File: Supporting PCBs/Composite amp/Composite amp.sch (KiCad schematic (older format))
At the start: 10 parts, among them J1 Conn_01x14_Female, Q1 MMBT3906

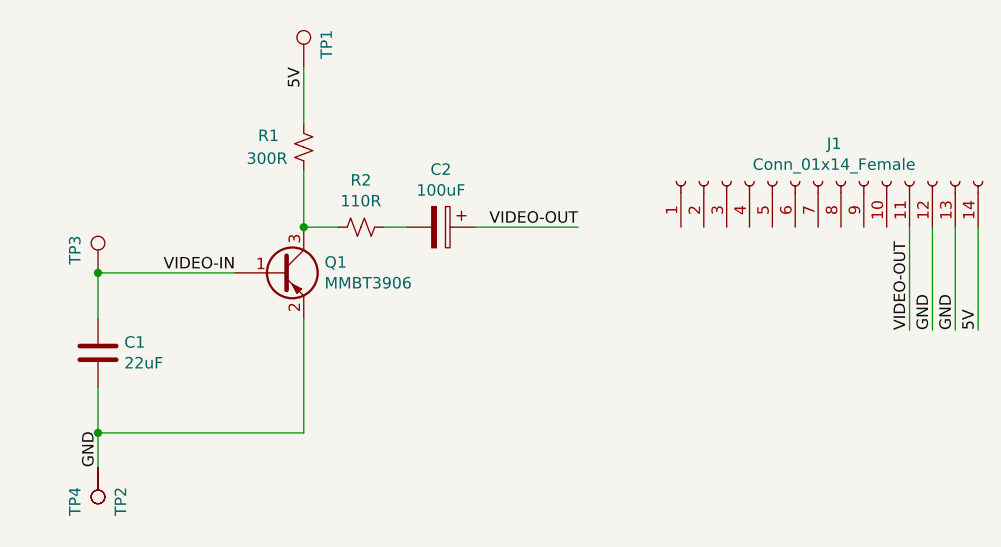
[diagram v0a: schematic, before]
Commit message: + Updated README.md + Fixed schematic/pinout error with Q1, and added decoupling capacitor to Composite Amp
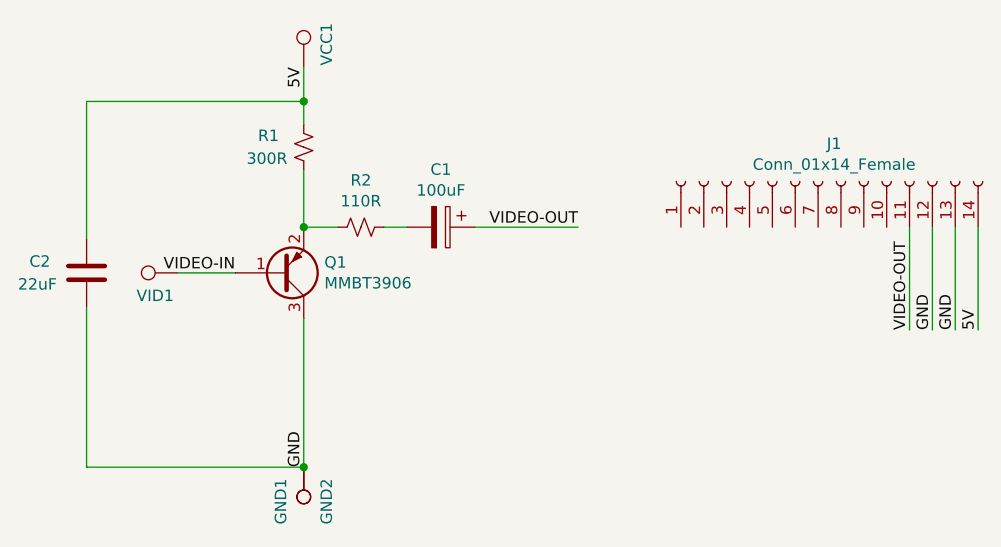
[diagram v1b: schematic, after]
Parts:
- removed C1: 22uF, Capacitor_SMD:C_0805_2012Metric, symbol Device:C
- added C2: 22uF, Capacitor_SMD:C_0805_2012Metric_Pad1.15x1.40mm_HandSolder, symbol Device:C
- renumbered C2 to C1, TP4 to GND1, TP2 to GND2, TP1 to VCC1, TP3 to VID1
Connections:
- net 5V: now also C2.1
- net GND: now also Q1.3 (C), C2.2; no longer Q1.2 (E)
- net at R1.2, R2.2: now also Q1.2 (E); no longer Q1.3 (C)
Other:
- moved on the sheet: GND1, GND2, VID1
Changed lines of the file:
@@
 Text Label 6300 2800 3    50   ~ 0
 5V
-Connection ~ 5400 4400
-Wire Wire Line
-	5400 4400 5400 4550
-Wire Wire Line
-	6300 3900 6300 4400
 $Comp
-L Connector:TestPoint TP2
+L Connector:TestPoint GND2
 U 1 1 6144479E
-P 5400 4550
-F 0 "TP2" V 5300 4700 50  0000 C CNN
-F 1 "TestPoint" V 5504 4622 50  0001 C CNN
-F 2 "TinyTendo:SolderPad" H 5600 4550 50  0001 C CNN
-F 3 "~" H 5600 4550 50  0001 C CNN
-	1    5400 4550
+P 6300 4550
+F 0 "GND2" V 6200 4700 50  0000 C CNN
+F 1 "TestPoint" V 6404 4622 50  0001 C CNN
+F 2 "TinyTendo:SolderPad" H 6500 4550 50  0001 C CNN
+F 3 "~" H 6500 4550 50  0001 C CNN
+	1    6300 4550
 	-1   0    0    1
 $EndComp
 $Comp
-L Connector:TestPoint TP3
+L Connector:TestPoint VID1
 U 1 1 61444DBD
-P 5400 3700
-F 0 "TP3" V 5300 3800 50  0000 C CNN
-F 1 "TestPoint" V 4400 3150 50  0001 C CNN
-F 2 "TinyTendo:SolderPad" H 5600 3700 50  0001 C CNN
-F 3 "~" H 5600 3700 50  0001 C CNN
-	1    5400 3700
-	1    0    0    -1
+P 5750 3700
+F 0 "VID1" V 5650 3800 50  0000 C CNN
+F 1 "TestPoint" V 4750 3150 50  0001 C CNN
+F 2 "TinyTendo:SolderPad" H 5950 3700 50  0001 C CNN
+F 3 "~" H 5950 3700 50  0001 C CNN
+	1    5750 3700
+	0    -1   -1   0
 $EndComp
 $Comp
@@
 5V
 Wire Wire Line
-	9050 3950 9050 3500
-Wire Wire Line
 	9150 3950 9150 3500
-Wire Wire Line
-	9250 3950 9250 3500
 Text Label 7500 3500 2    50   ~ 0
 VIDEO-OUT
@@
 Text Label 9150 3950 1    50   ~ 0
 GND
-Wire Wire Line
-	8950 3950 8950 3500
 Text Label 8950 3950 1    50   ~ 0
 VIDEO-OUT
 $Comp
-L Connector:TestPoint TP4
+L Connector:TestPoint GND1
 U 1 1 6142B86A
-P 5400 4550
-F 0 "TP4" V 5500 4700 50  0000 C CNN
-F 1 "TestPoint" V 5504 4622 50  0001 C CNN
-F 2 "TinyTendo:SolderPad" H 5600 4550 50  0001 C CNN
-F 3 "~" H 5600 4550 50  0001 C CNN
-	1    5400 4550
+P 6300 4550
+F 0 "GND1" V 6400 4700 50  0000 C CNN
+F 1 "TestPoint" V 6404 4622 50  0001 C CNN
+F 2 "TinyTendo:SolderPad" H 6500 4550 50  0001 C CNN
+F 3 "~" H 6500 4550 50  0001 C CNN
+	1    6300 4550
 	-1   0    0    1
 $EndComp
+Text Label 6300 4550 1    50   ~ 0
+GND
+Text Label 6000 3700 2    50   ~ 0
+VIDEO-IN
+Wire Wire Line
+	6300 2800 6300 2950
+Wire Wire Line
+	7050 3500 7500 3500
 $Comp
-L Device:C C1
-U 1 1 60214EBB
-P 5400 4050
-F 0 "C1" H 5515 4096 50  0000 L CNN
-F 1 "22uF" H 5515 4005 50  0000 L CNN
-F 2 "Capacitor_SMD:C_0805_2012Metric" H 5438 3900 50  0001 C CNN
-F 3 "~" H 5400 4050 50  0001 C CNN
-	1    5400 4050
-	1    0    0    -1
+L Device:CP C1
+U 1 1 6021CE25
+P 6900 3500
+F 0 "C1" V 6648 3500 50  0000 C CNN
+F 1 "100uF" V 6739 3500 50  0000 C CNN
+F 2 "Capacitor_SMD:CP_Elec_4x4.5" H 6938 3350 50  0001 C CNN
+F 3 "~" H 6900 3500 50  0001 C CNN
+	1    6900 3500
+	0    1    1    0
 $EndComp
+Connection ~ 6300 3500
+$Comp
+L Transistor_BJT:MMBT3906 Q1
+U 1 1 6022F5A4
+P 6200 3700
+F 0 "Q1" H 6390 3654 50  0000 L CNN
+F 1 "MMBT3906" H 6390 3745 50  0000 L CNN
+F 2 "Package_TO_SOT_SMD:SOT-23" H 6400 3625 50  0001 L CIN
+F 3 "https://www.fairchildsemi.com/datasheets/2N/2N3906.pdf" H 6200 3700 50  0001 L CNN
+	1    6200 3700
+	1    0    0    1
+$EndComp
+Connection ~ 6300 4550
 Wire Wire Line
-	5400 4400 6300 4400
-Wire Wire Line
-	5400 4200 5400 4400
-Wire Wire Line
-	5400 3900 5400 3700
-Wire Wire Line
-	5400 3700 6000 3700
-Connection ~ 5400 3700
-Text Label 5400 4550 1    50   ~ 0
-GND
+	6300 3900 6300 4550
 $Comp
-L Connector:TestPoint TP1
+L Connector:TestPoint VCC1
 U 1 1 61444261
 P 6300 2800
-F 0 "TP1" V 6400 2900 50  0000 C CNN
+F 0 "VCC1" V 6400 2900 50  0000 C CNN
 F 1 "TestPoint" V 6404 2872 50  0001 C CNN
 F 2 "TinyTendo:SolderPad" H 6500 2800 50  0001 C CNN
@@
 	1    0    0    -1
 $EndComp
-Text Label 6000 3700 2    50   ~ 0
-VIDEO-IN
-Wire Wire Line
-	6300 2800 6300 3050
-Wire Wire Line
-	7050 3500 7500 3500
 $Comp
-L Device:CP C2
-U 1 1 6021CE25
-P 6900 3500
-F 0 "C2" V 6648 3500 50  0000 C CNN
-F 1 "100uF" V 6739 3500 50  0000 C CNN
-F 2 "Capacitor_SMD:CP_Elec_4x4.5" H 6938 3350 50  0001 C CNN
-F 3 "~" H 6900 3500 50  0001 C CNN
-	1    6900 3500
-	0    1    1    0
-$EndComp
-$Comp
-L Transistor_BJT:MMBT3906 Q1
-U 1 1 627580CD
-P 6200 3700
-F 0 "Q1" H 6391 3746 50  0000 L CNN
-F 1 "MMBT3906" H 6391 3655 50  0000 L CNN
-F 2 "Package_TO_SOT_SMD:SOT-23" H 6400 3625 50  0001 L CIN
-F 3 "https://www.fairchildsemi.com/datasheets/2N/2N3906.pdf" H 6200 3700 50  0001 L CNN
-	1    6200 3700
+L Device:C C2
+U 1 1 62935BB3
+P 5350 3700
+F 0 "C2" H 5100 3750 50  0000 L CNN
+F 1 "22uF" H 5050 3650 50  0000 L CNN
+F 2 "Capacitor_SMD:C_0805_2012Metric_Pad1.15x1.40mm_HandSolder" H 5388 3550 50  0001 C CNN
+F 3 "~" H 5350 3700 50  0001 C CNN
+	1    5350 3700
 	1    0    0    -1
 $EndComp
-Connection ~ 6300 3500
+Wire Wire Line
+	8950 3950 8950 3500
+Wire Wire Line
+	9050 3950 9050 3500
+Wire Wire Line
+	9250 3500 9250 3950
+Wire Wire Line
+	5350 3550 5350 2950
+Connection ~ 6300 2950
+Wire Wire Line
+	6300 2950 6300 3050
+Wire Wire Line
+	5350 3850 5350 4550
+Wire Wire Line
+	5750 3700 6000 3700
+Wire Wire Line
+	5350 2950 6300 2950
+Wire Wire Line
+	5350 4550 6300 4550
 $EndSCHEMATC
